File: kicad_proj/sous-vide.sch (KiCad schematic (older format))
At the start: 29 parts, among them J1 Heater, J2 Power, J3 Conn_01x02, J4 Jumper, J5 Jumper, Q1 2N3904, SW1 SW_Push_Dual, SW2 SW_Push_Dual, U1 G5LE, U2 RAC01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

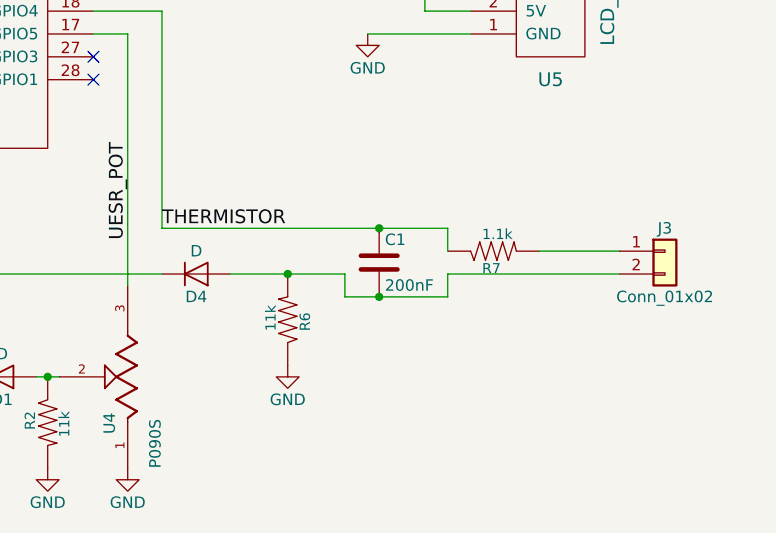
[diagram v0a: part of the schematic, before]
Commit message: turns out I got the thermistor circuit wrong
so I updated the schematic even though I'm definitely not ordering a new board just for that.
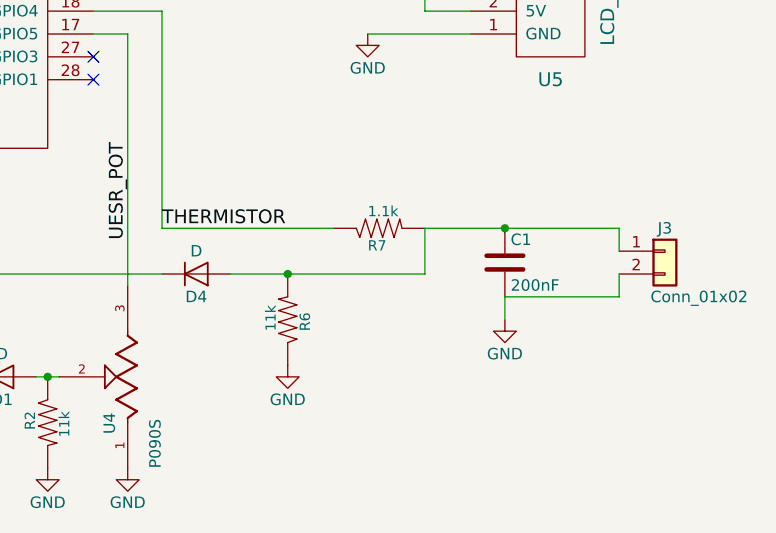
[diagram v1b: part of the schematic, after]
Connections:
- net GND: now also C1.2, J3.2 (Pin_2)
- net THERMISTOR: no longer C1.1
- net at D4.2 (A), R6.2: now also C1.1, J3.1 (Pin_1), R7.2; no longer C1.2, J3.2 (Pin_2)
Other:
- moved on the sheet: C1, R7
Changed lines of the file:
@@
 LIBS:contrib
 LIBS:valves
-LIBS:misc
-LIBS:nodemcu
-LIBS:sensors
-LIBS:NodeMCU_TEMPLATE
 LIBS:SparkFun-Aesthetics
 LIBS:SparkFun-Batteries
@@
 LIBS:SparkFun-Sensors
 LIBS:SparkFun-Switches
-LIBS:rac01
-LIBS:g5le
-LIBS:node_mcu1
-LIBS:lcd_backpack
-LIBS:P090S-04F20BR10K
 LIBS:sous-vide-cache
 EELAYER 25 0
@@
 P 8850 5350
 F 0 "J3" H 8850 5450 50  0000 C CNN
-F 1 "Conn_01x02" H 8850 5150 50  0000 C CNN
+F 1 "Conn_01x02" H 9000 5150 50  0000 C CNN
 F 2 "Pin_Headers:Pin_Header_Straight_1x02_Pitch2.54mm" H 8850 5350 50  0001 C CNN
 F 3 "" H 8850 5350 50  0001 C CNN
@@
 L C C1
 U 1 1 5A494F7C
-P 7600 5400
-F 0 "C1" H 7625 5500 50  0000 L CNN
-F 1 "200nF" H 7625 5300 50  0000 L CNN
-F 2 "Capacitors_THT:C_Disc_D4.3mm_W1.9mm_P5.00mm" H 7638 5250 50  0001 C CNN
-F 3 "" H 7600 5400 50  0001 C CNN
-	1    7600 5400
+P 8150 5400
+F 0 "C1" H 8175 5500 50  0000 L CNN
+F 1 "200nF" H 8175 5300 50  0000 L CNN
+F 2 "Capacitors_THT:C_Disc_D4.3mm_W1.9mm_P5.00mm" H 8188 5250 50  0001 C CNN
+F 3 "" H 8150 5400 50  0001 C CNN
+	1    8150 5400
 	1    0    0    -1
 $EndComp
@@
 L RESISTOR0402 R7
 U 1 1 5A496D58
-P 8100 5350
-F 0 "R7" H 8050 5400 45  0000 L BNN
-F 1 "1.1k" H 8050 5250 45  0000 L BNN
-F 2 "Resistors_THT:R_Axial_DIN0207_L6.3mm_D2.5mm_P10.16mm_Horizontal" H 8100 5500 20  0001 C CNN
-F 3 "" H 8100 5350 60  0001 C CNN
-F 4 " " H 8100 5550 60  0000 C CNN "Field4"
-	1    8100 5350
+P 7600 5250
+F 0 "R7" H 7550 5300 45  0000 L BNN
+F 1 "1.1k" H 7550 5150 45  0000 L BNN
+F 2 "Resistors_THT:R_Axial_DIN0207_L6.3mm_D2.5mm_P10.16mm_Horizontal" H 7600 5400 20  0001 C CNN
+F 3 "" H 7600 5250 60  0001 C CNN
+F 4 " " H 7600 5450 60  0000 C CNN "Field4"
+	1    7600 5250
 	1    0    0    1
 $EndComp
@@
 Text Label 5550 1800 2    60   ~ 0
 -coil
-Wire Wire Line
-	6950 5450 7450 5450
 Connection ~ 7200 5450
 Wire Wire Line
@@
 	4250 3650 4450 3650
 Wire Wire Line
-	6650 5250 7900 5250
-Wire Wire Line
-	7900 5250 7900 5350
-Wire Wire Line
-	7450 5550 7900 5550
-Wire Wire Line
-	7900 5550 7900 5450
-Wire Wire Line
-	7450 5450 7450 5550
-Connection ~ 7600 5550
-Wire Wire Line
-	7450 5250 7450 5250
-Connection ~ 7600 5250
-Wire Wire Line
-	7900 5450 8650 5450
-Wire Wire Line
-	8300 5350 8650 5350
-Wire Wire Line
 	5750 2250 5750 2500
 Wire Wire Line
@@
 	3450 2000 3450 1450
 Connection ~ 3450 1450
+Wire Wire Line
+	6950 5450 7800 5450
+Wire Wire Line
+	6650 5250 7400 5250
+Wire Wire Line
+	7800 5250 8650 5250
+Wire Wire Line
+	7800 5450 7800 5250
+Wire Wire Line
+	8650 5250 8650 5350
+Connection ~ 8150 5250
+Wire Wire Line
+	8650 5450 8650 5550
+Wire Wire Line
+	8650 5550 8150 5550
+$Comp
+L GND #PWR?
+U 1 1 5A6ED1AF
+P 8150 5650
+F 0 "#PWR?" H 8150 5400 50  0001 C CNN
+F 1 "GND" H 8150 5500 50  0000 C CNN
+F 2 "" H 8150 5650 50  0001 C CNN
+F 3 "" H 8150 5650 50  0001 C CNN
+	1    8150 5650
+	1    0    0    -1
+$EndComp
+Wire Wire Line
+	8150 5550 8150 5650
 $EndSCHEMATC
